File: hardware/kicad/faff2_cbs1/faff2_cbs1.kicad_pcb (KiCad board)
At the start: 4 copper layers, 210 x 130 mm, 412 parts, among them J1001 USB_C_Receptacle_USB2.0_16P, J1002 TSW-105-07-F-D, J1003 SAMTEC_SHF-107-01-L-D-SM, J1101 1x6 2.54mm, J1102 1x6 2.54mm, J1103 Micro-Fit 1x3, J201 KPJX-4S, J301 PH1-06-UA, J501 1729076, J502 8510-4500PL, J503 CONUFL001-SMD, J504 CONUFL001-SMD, J601 FH12-10S-0.5SH(55), J602 FTSH-105-01-L-DV-K-TR, J603 8510-4500PL, J701 1752120, J702 1752120, J703 8510-4500PL, J901 BTN EXT, J902 SMA Jack, J903 J-LIM, Q1101 BSZ099N06LS5, Q1102 BSZ099N06LS5, Q1103 BSZ099N06LS5, Q1104 BSZ099N06LS5, Q1105 BSZ099N06LS5, Q1106 BSZ099N06LS5, Q201 DMP6023LFG-7, SW1001 PTS526, SW901 PTS526, SW902 PTS526, SW903 PTS526, SW904 PTS526, U1001 STM32H723VET6, U1002 USB3320C, U1003 SRAM 32Mb, U1004 MIC5365-1.8, U1101 DRV8323S, U301 LMR33630, U302 ADPL42005, U303 ADPL42005, U304 LMR33630, U501 ADS1235, U601 AM26LV32, U701 ADS1120, U801 24FC16T-I/OT, U901 SN74LVC1G17, U902 SN74LVC1G11, Y1001 24MHz, Y1002 24MHz 18pF

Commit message: pcb: placement round 1 - all 412 footprints placed, nothing routed
Executes the edge plan of docs/decisions/actuator-pcb-setup.md S5. Actuator
edge (y=160) carries the nine actuator connectors, bench edge (y=30) the five
bench ones; the load-cell AFE and temp sense take the far bottom-left corner,
the MCU the centre, and the 24 V entry, both bucks, both LDOs and the motor
bridge the right-hand column - diagonally opposite the analog corner.

The motor bridge is three vertical half-bridge legs at 15 mm pitch (W, V, U
left to right), current reading top to bottom: DC-link store -> V24_MOT rail
-> Q_high -> phase -> Q_low -> shunt -> GND plane, with the DRV8323S directly
below so SPI, ENABLE, nFAULT and the three current senses leave west into the
MCU corridor. Each leg has its own 2.2 uF + 100 nF bypass pair beside its
drain; RT1101 sits inside the FET field.

Both switcher input capacitors straddle their regulator's adjacent VIN/GND
pin pair side by side - 2.81 mm supply, 2.80 mm return - and both inductors
are oriented by pad net so the SW terminal is 3.4-3.8 mm from the SW pin.
Every MCU VDD/VSS pair carries its own 100 nF at 3.5-4.2 mm on both links.
Median decoupler link over the whole board is 4.52 mm.

Verification: schematic parity 0; real-courtyard overlaps 0; board-edge and
M3 keep-out margin 0 findings; 0.25 mm grid 0 findings; silkscreen 0 (149
overlaps at first placement, all re-seated, and 0.7 mm library text lifted to
the 0.8 mm house floor on the board). DRC is 19 violations, every one of them
a pre-existing library residual recorded in board setup S8, plus 499
unconnected items, which is the whole ratsnest. 0 tracks, 0 vias, 0 zones -
G7 is a hard gate and the captain reviews placement before any routing.
Schematic ERC re-run after the board saves: still 0/0.

Five open points are listed for the captain, the first being the 13-27 mm
gate runs that three-legs-in-a-row forces, with the L-fold alternative.

Co-Authored-By: Claude Opus 5 <noreply@anthropi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
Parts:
- moved TP1111 454.5 mm to (173.0, 145.0)
- moved TP1108 453.6 mm to (181.5, 110.0)
- moved TP1110 453.3 mm to (169.5, 145.0)
- moved TP1103 437.9 mm to (178.0, 110.0)
- moved TP1109 435.5 mm to (187.5, 141.0)
- moved TP1101 429.4 mm to (181.5, 100.5)
- moved TP1102 429.0 mm to (186.0, 105.5)
- moved TP1105 415.7 mm to (185.5, 151.5)
- moved TP1104 391.0 mm to (229.5, 126.0)
- moved RT1101 390.7 mm to (205.5, 126.0)
- moved Y1002 387.8 mm to (140.5, 55.5), turned to 90 degrees
- moved TP1107 386.0 mm to (234.0, 146.5)
- moved TP1106 385.4 mm to (230.0, 146.5)
- moved U1003 384.2 mm to (131.0, 52.0)
- moved R1130 380.5 mm to (175.0, 153.5), turned to 90 degrees
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
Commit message: pcb: routing step 1 - the two internal GND planes
House process step 1: establish the ground planes before any track. Full GND
fill on In1.Cu and In2.Cu at 0.15 mm minimum width, 0.15 mm clearance, 0.25 mm
corner fillet, islands always removed, thermal-relief pad connections (G1/G10:
unbroken, never split).

Each plane fills as a single outline of 26342 mm^2 -- one continuous pour.
DRC unchanged at the 19 known library residuals; unconnected drops from 499 to
499 total but GND's share falls 276 -> 108 as every PTH GND barrel now reaches
the planes.

Co-Authored-By: Claude Opus 5 <noreply@anthropic.com>
Claude-Session: https://claude.ai/code/session_017ffYKyG4Q48Dk1cCPgUL7k
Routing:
- added copper zone on In1.Cu, net GND
- added copper zone on In2.Cu, net GND
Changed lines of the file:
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@@
+		)
+	)
+	(zone
+		(net 118)
+		(net_name "GND")
+		(layer "In1.Cu")
+		(hatch edge 0.5)
+		(connect_pads
+			(clearance 0.15)
+		)
+		(min_thickness 0.15)
+		(filled_areas_thickness no)
+		(fill yes
+			(thermal_gap 0.5)
+			(thermal_bridge_width 0.5)
+			(smoothing fillet)
+			(radius 0.25)
+		)
+		(polygon
+			(pts
+				(xy 30 30) (xy 240 30) (xy 240 160) (xy 30 160)
+			)
+		)
+	)
+	(zone
+		(net 118)
+		(net_name "GND")
+		(layer "In2.Cu")
+		(hatch edge 0.5)
+		(connect_pads
+			(clearance 0.15)
+		)
+		(min_thickness 0.15)
+		(filled_areas_thickness no)
+		(fill yes
+			(thermal_gap 0.5)
+			(thermal_bridge_width 0.5)
+			(smoothing fillet)
+			(radius 0.25)
+		)
+		(polygon
+			(pts
+				(xy 30 30) (xy 240 30) (xy 240 160) (xy 30 160)
+			)
 		)
 	)

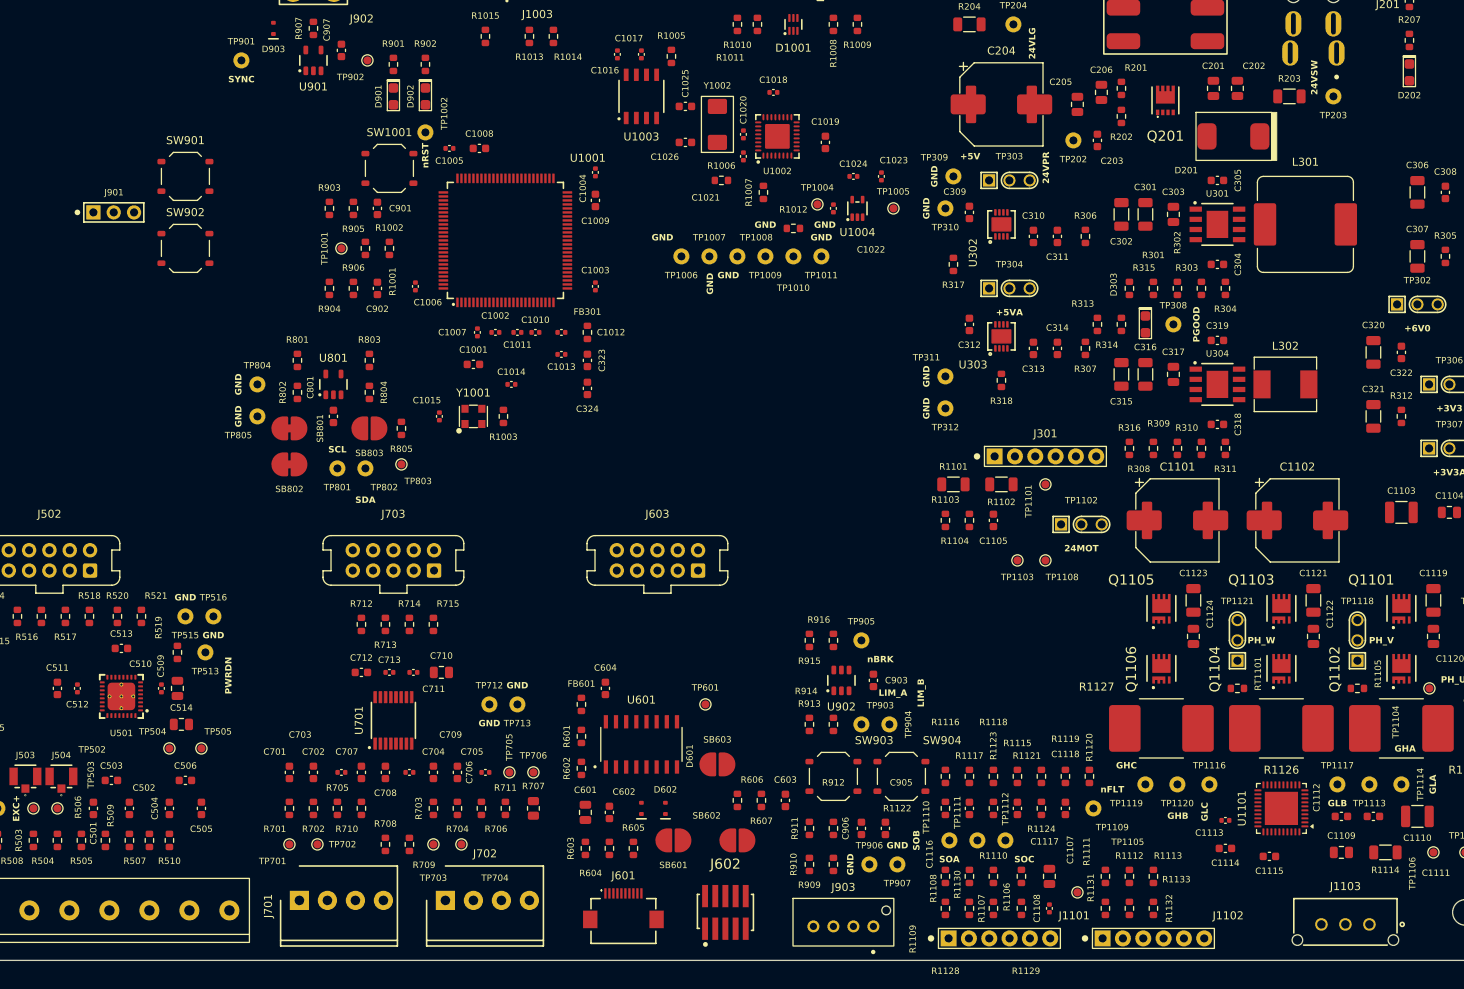
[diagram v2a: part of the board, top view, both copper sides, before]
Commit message: pcb: routing step 2 - positive feeds to every decoupling capacitor
House flow (VanClock R1-3/R1-4): feed via -> capacitor pad -> IC pin, never
pin-first, never a stub. Via->cap-pad trace at the via outer diameter (0.6 mm);
cap-pad->pin link at the IC pin-pad width. 55 decouplers fed, 49 feed vias;
nearest cap to each pin routed first so a second cap on the same pin chains
onto the link rather than being swept over by it.

Two carve-outs the skill itself allows, both recorded in the script header:
27 source-chain caps (24 V entry, both buck output nodes, both LDO outputs,
the +3V3A filter and the whole V24_MOT bridge rail) keep their feed in-line on
the outer layer and are routed in step 4; six two-node cap nets (C304, C318,
C513, C1008, C1009, C1115) have no distribution to feed them, so they get the
in-line link only.

Also adds tools/route_lib.py - the obstacle model (real pad/track/via/hole/
keep-out copper, per-net, per-layer), the two-layer A* maze router and the
board constants read from this project's own .kicad_pro.

DRC: the 19 known library residuals plus 49 via_dangling - the feed vias
waiting for step 4's rail distribution, which the house process calls a
documented in-progress residual, not a defect.

Co-Authored-By: Claude Opus 5 <noreply@anthropic.com>
Claude-Session: https://claude.ai/code/session_017ffYKyG4Q48Dk1cCPgUL7k
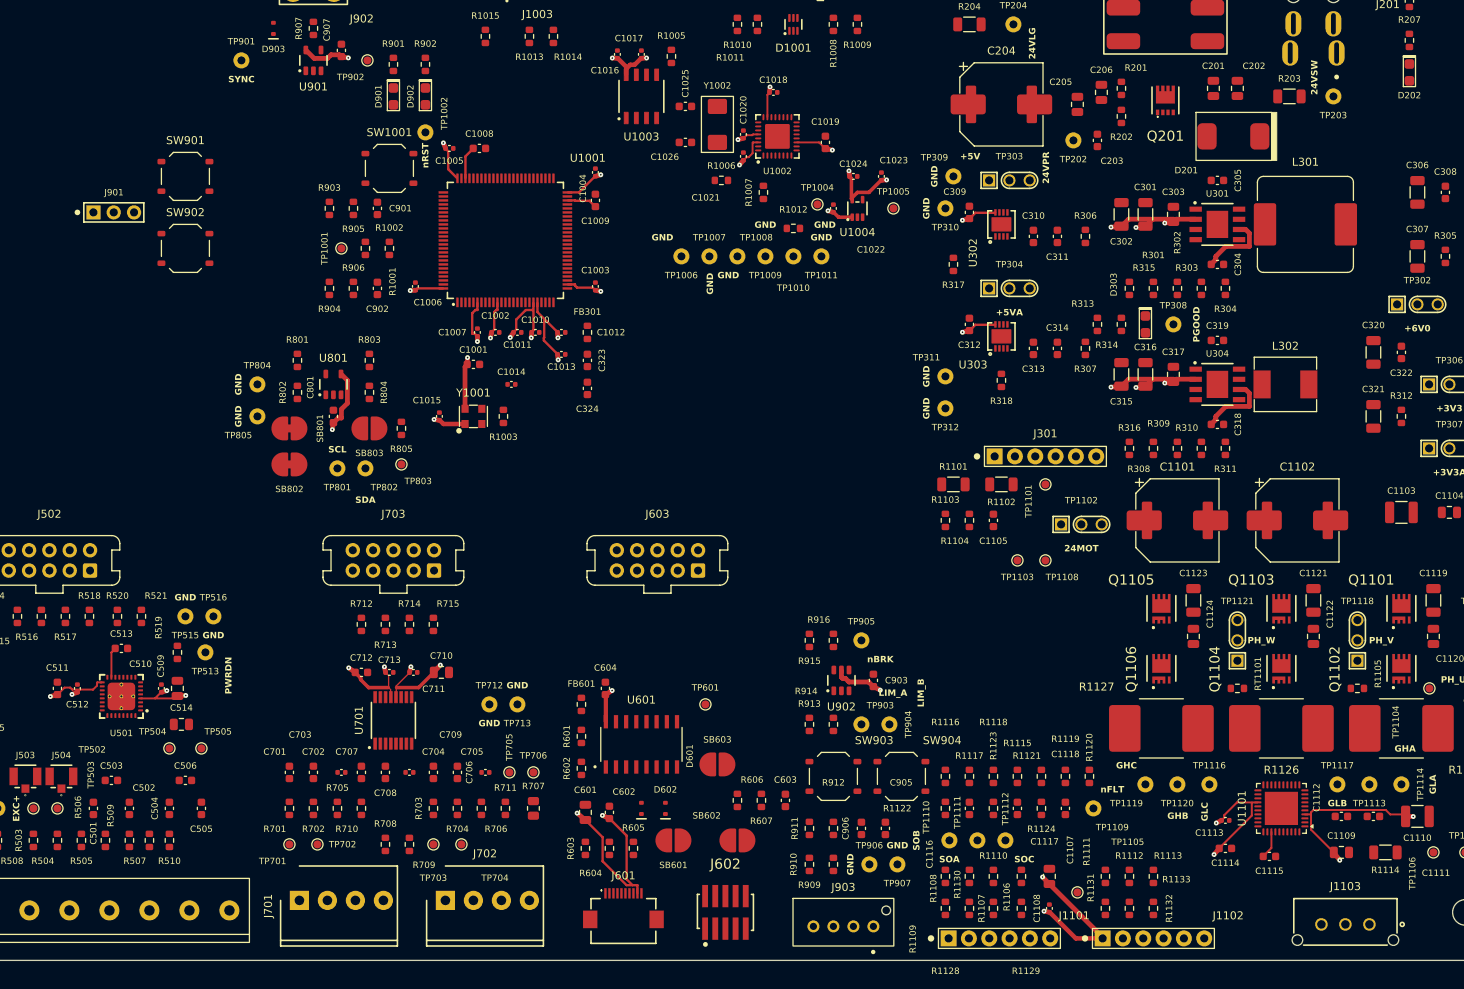
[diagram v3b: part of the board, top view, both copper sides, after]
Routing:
- net +3V3: track 0.00 -> 102.8 mm, vias 0 -> 20
- net /power_entry_24v/V24_LOGIC: track 0.00 -> 28.4 mm, vias 0 -> 6
- net /linear_encoder/+5V_ENC: track 0.00 -> 24.2 mm, vias 0 -> 2
- net /motor_drive/VM_DRV: track 0.00 -> 20.7 mm, vias 0 -> 2
- net +3V3A: track 0.00 -> 20.4 mm, vias 0 -> 4
- net /motor_drive/VENC: track 0.00 -> 19.1 mm, vias 0 -> 2
- net +5VA: track 0.00 -> 18.3 mm, vias 0 -> 4
- net /mcu/+1V8_USB: track 0.00 -> 15.6 mm, vias 0 -> 4
- net /mcu/+3V3_USB: track 0.00 -> 11.7 mm, vias 0 -> 3
- net Net-(U304-VCC): track 0.00 -> 8.98 mm
- net Net-(U301-VCC): track 0.00 -> 8.98 mm
- net /power_rails/+6V0: track 0.00 -> 8.67 mm, vias 0 -> 2
- net Net-(C1008-Pad1): track 0.00 -> 4.04 mm
- net Net-(C1009-Pad1): track 0.00 -> 3.71 mm
- net Net-(U501A-BYPASS): track 0.00 -> 3.69 mm
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
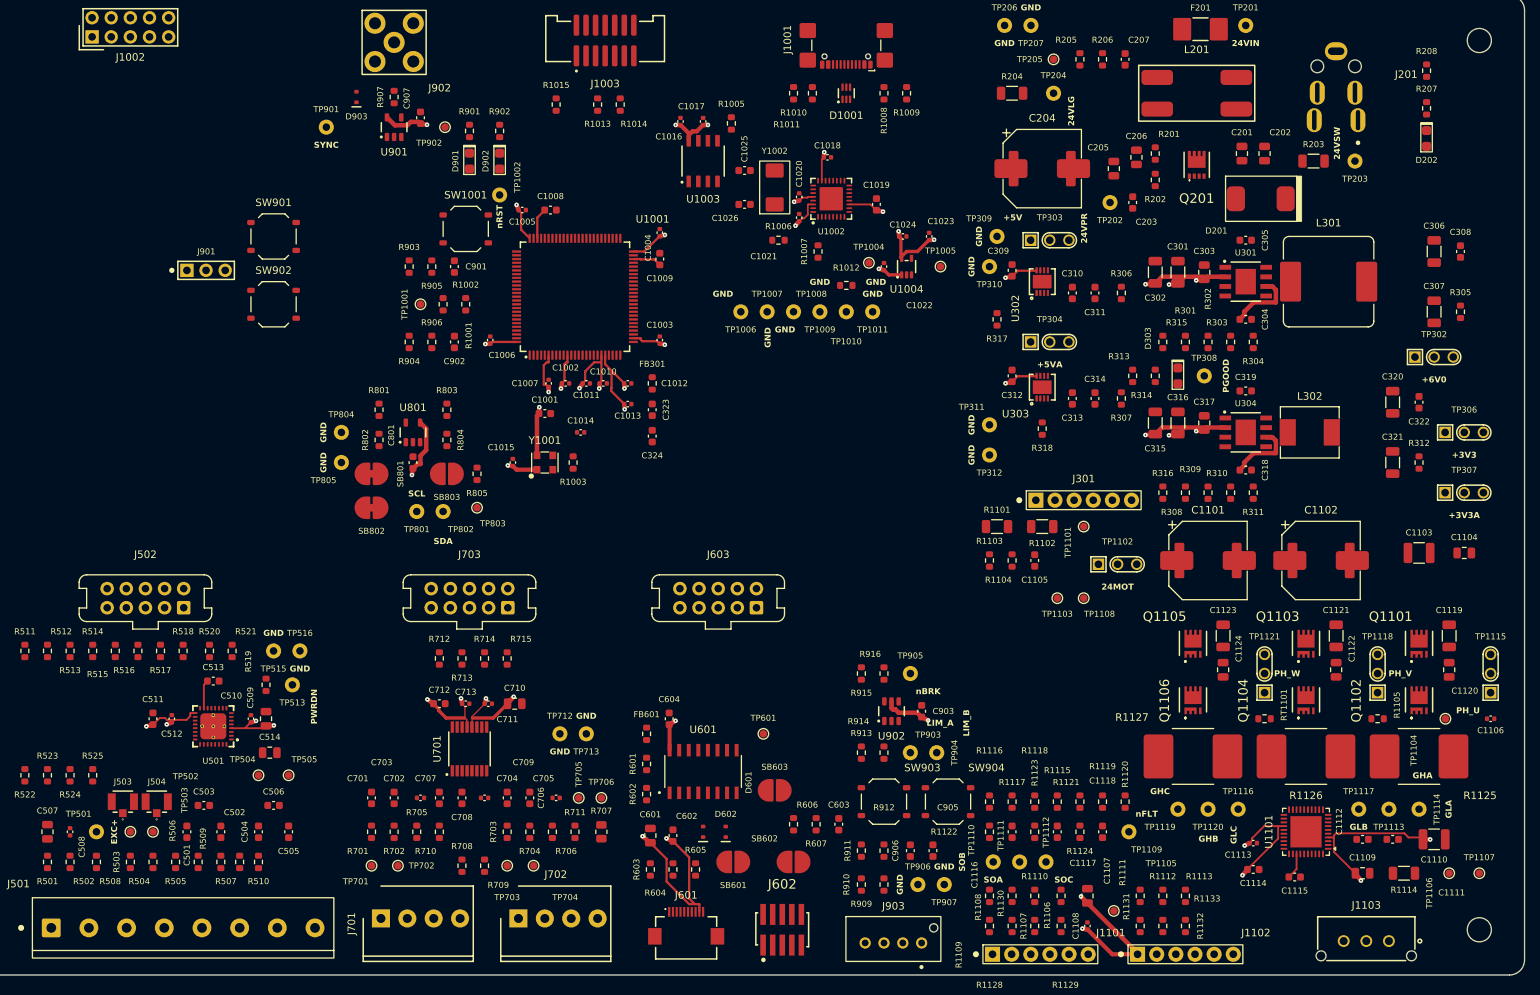
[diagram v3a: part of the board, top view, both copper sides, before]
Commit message: pcb: routing step 3 - one GND via per pad, and the completeness proof
House rule: every GND pin gets its OWN via, never one shared between two
ground pads - a shared via puts its inductance inside both capacitors' loops
(Bogatin p.344). 214 SMD GND pads in 209 lands; 208 lands stitched, 254 GND
vias; the 63 PTH GND pads reach both planes through their own barrels.

No via-in-pad: the seven IC exposed pads carry the client-ruled G9 array (29
in-pad vias); every other big ground land - the three shunts, the DC-link
cans, the TVS, the common-mode choke, the FPC shells - takes a fan of vias
*beside* the pad, sized from the 1.0 A/via budget, so nothing wicks solder
into a barrel. tools/route_check.py --viainpad proves it by true rectangle
distance: 0 vias in any other pad.

Two things the engineer should see, both printed by the stage:
* 8 vias could not take their pin's in-line lane and were swung (R3-1 says log
  these); five are LQFP100 VSS pins whose via sits inside the package outline
  because the neighbouring decoupler link owns the outward lane.
* 4 pins had no in-line lane at all and take a short maze-routed stub to a
  nearby slot: U1101.32, U501.5, U701.5, C1010.2.

D1001's GND pin is deliberately deferred to step 5: it sits *between* the two
USB data lines, so its via and the pair's local spread have to be drawn
together. The controlled-impedance corridors are reserved in the obstacle
model before stitching so a ground via cannot land in the pair's only run -
one did, twice, before the reservation went in.

Also fixes two obstacle-model defects found by the proofs: a 45 deg track
segment was blocking its whole bbox (0.4 mm of phantom copper, which walled
off legal lanes), and step 2's feed-via slot was sized from the pad's
unrotated size, so on a 90 deg rotated cap the via landed 0.02 mm inside its
own pad.

DRC: the 19 known library residuals plus 49 via_dangling (step 2's feed vias,
still waiting for step 4). Schematic parity 0.

Co-Authored-By: Claude Opus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
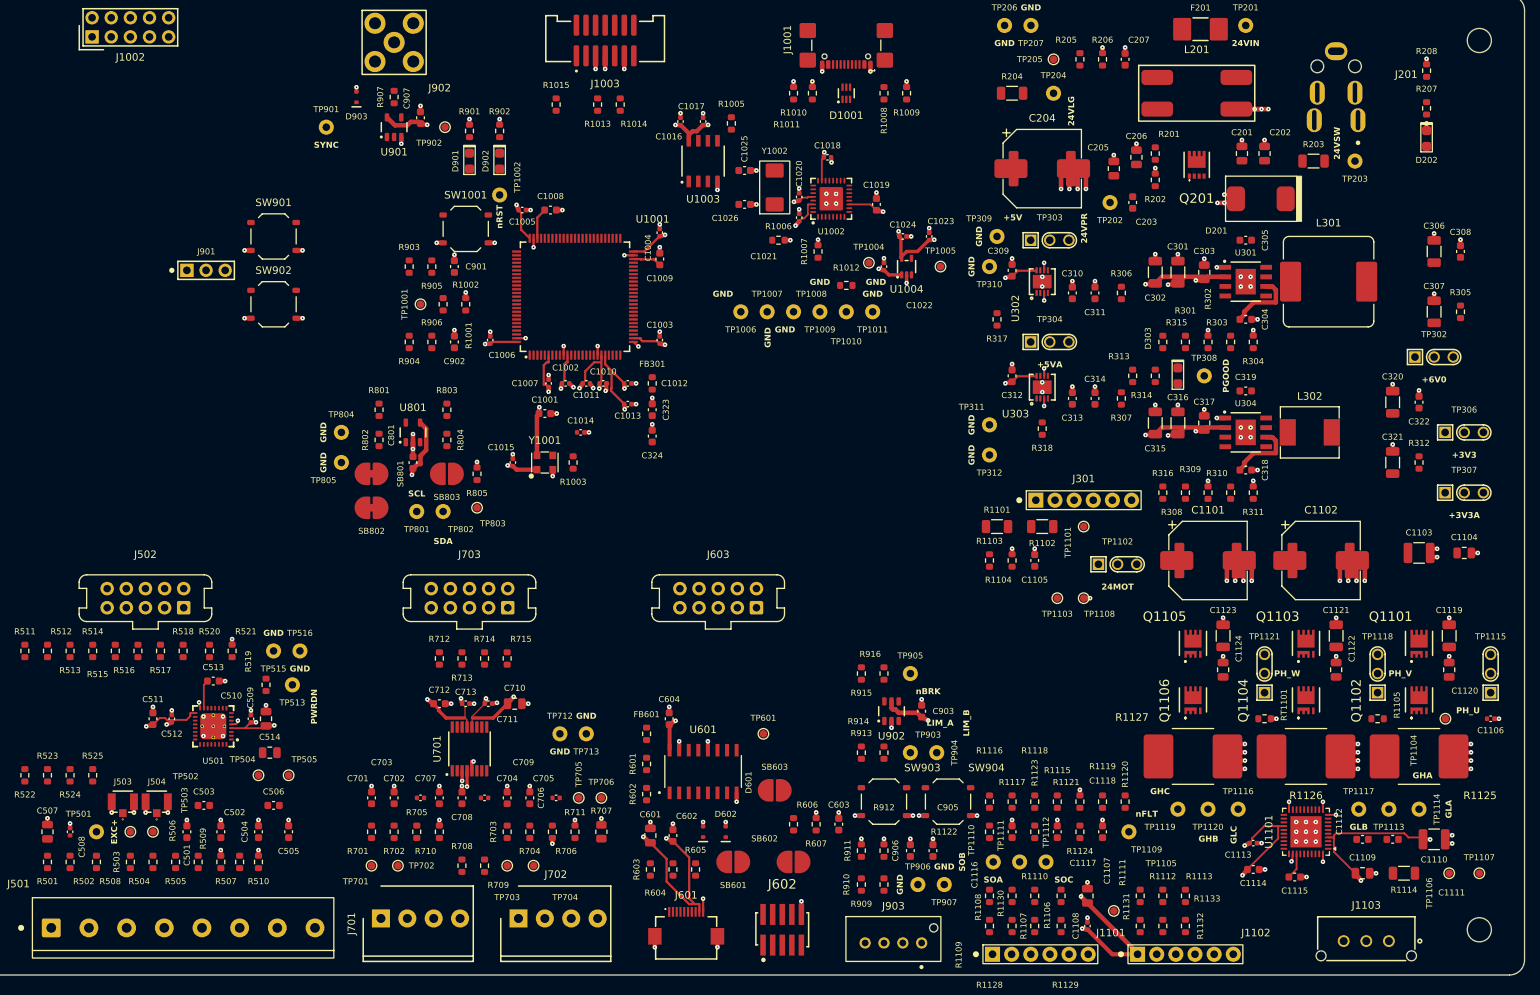
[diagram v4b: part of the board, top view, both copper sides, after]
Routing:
- net GND: track 0.00 -> 249.8 mm, vias 0 -> 254
